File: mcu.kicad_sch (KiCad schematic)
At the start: 19 parts, among them J1 Conn_01x04, U1 STM32G473CCUx, Y1 8 MHz

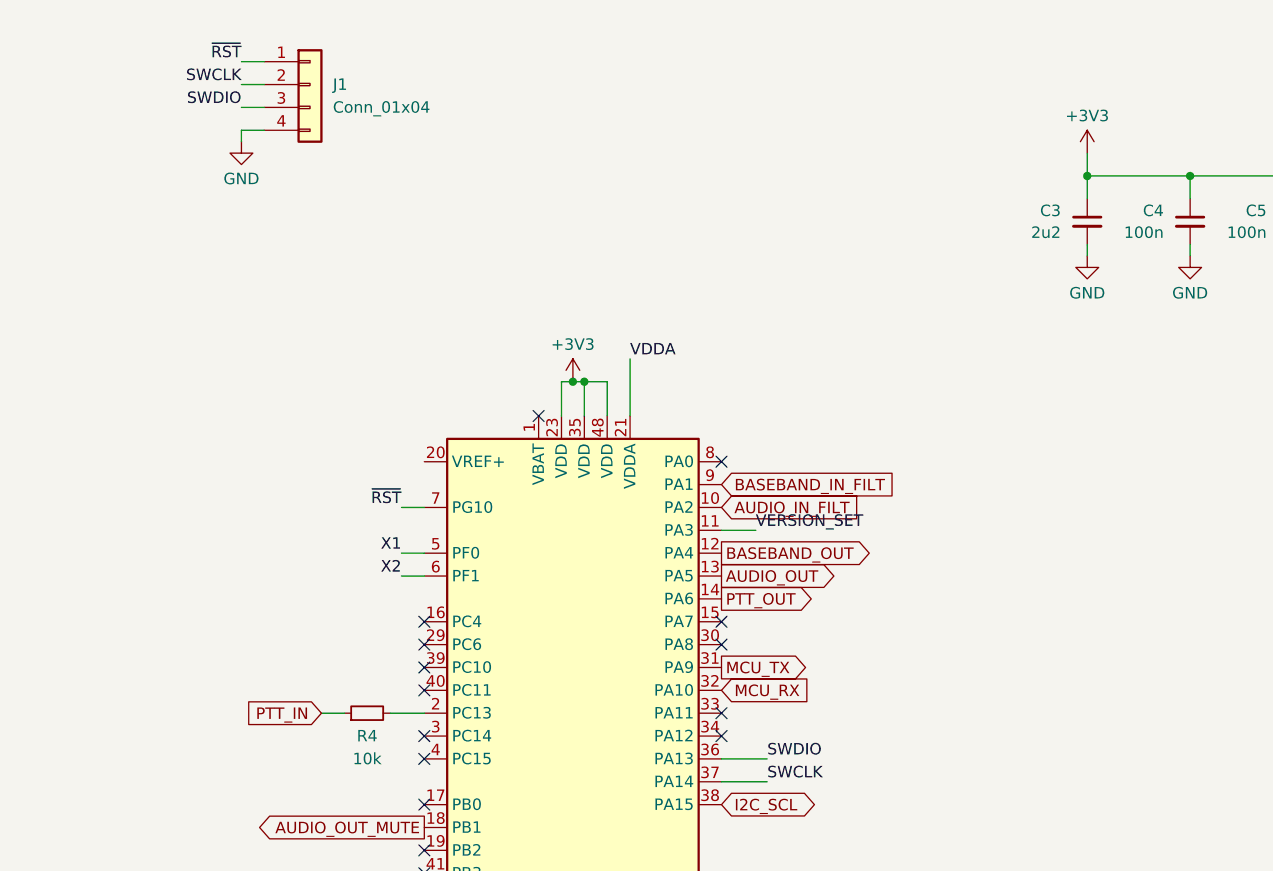
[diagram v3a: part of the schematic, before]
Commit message: Updates
GP relay added,
3v3 added to programming conn.
diode(dnp) added for motorola type internal bus.
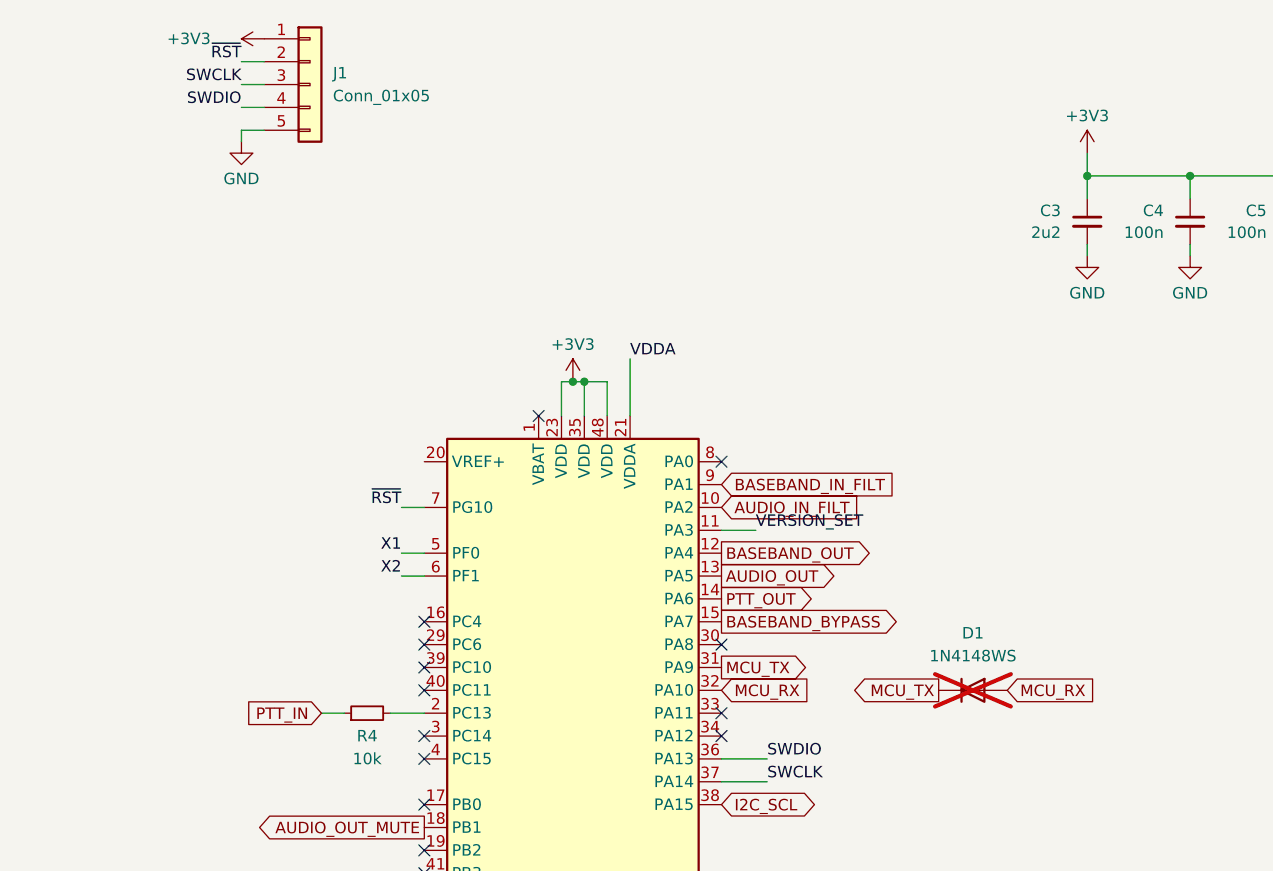
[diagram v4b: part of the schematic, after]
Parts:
- removed J1: Conn_01x04, Connector_Harwin:Harwin_M20-89004xx_1x04_P2.54mm_Horizontal, symbol Connector_Generic:Conn_01x04
- added D1: 1N4148WS, Diode_SMD:D_SOD-323, symbol Diode:1N4148WS
- added J1: Conn_01x05, Connector_Harwin:Harwin_M20-89005xx_1x05_P2.54mm_Horizontal, symbol Connector_Generic:Conn_01x05
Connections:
- net +3V3: now also J1.1 (Pin_1)
- net GND: now also J1.5 (Pin_5)
- net MCU_RX: now also D1.2 (A)
- net MCU_TX: now also D1.1 (K)
- net SWCLK: now also J1.3 (Pin_3)
- net SWDIO: now also J1.4 (Pin_4)
- net ~{RST}: now also J1.2 (Pin_2)
- net BASEBAND_BYPASS: now reaches U1.15 (PA7)
- no-connect marks 25 -> 24
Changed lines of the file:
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@@
 	)
 	(no_connect
-		(at 154.94 83.82)
-	)
-	(no_connect
 		(at 121.92 121.92)
 	)
@@
 		)
 	)
+	(global_label "MCU_TX"
+		(shape output)
+		(at 179.07 91.44 180)
+		(fields_autoplaced yes)
+		(effects
+			(font
+				(size 1.27 1.27)
+			)
+			(justify right)
+		)
+		(property "Intersheetrefs" "${INTERSHEET_REFS}"
+			(at 168.8882 91.44 0)
+			(effects
+				(font
+					(size 1.27 1.27)
+				)
+				(justify right)
+				(hide yes)
+			)
+		)
+	)
+	(global_label "BASEBAND_BYPASS"
+		(shape output)
+		(at 154.94 83.82 0)
+		(fields_autoplaced yes)
+		(effects
+			(font
+				(size 1.27 1.27)
+			)
+			(justify left)
+		)
+		(property "Intersheetrefs" "${INTERSHEET_REFS}"
+			(at 175.7052 83.82 0)
+			(effects
+				(font
+					(size 1.27 1.27)
+				)
+				(justify left)
+				(hide yes)
+			)
+		)
+	)
 	(global_label "AUDIO_OUT_MUTE"
 		(shape output)
@@
 		)
 	)
+	(global_label "MCU_RX"
+		(shape input)
+		(at 186.69 91.44 0)
+		(fields_autoplaced yes)
+		(effects
+			(font
+				(size 1.27 1.27)
+			)
+			(justify left)
+		)
+		(property "Intersheetrefs" "${INTERSHEET_REFS}"
+			(at 197.1742 91.44 0)
+			(effects
+				(font
+					(size 1.27 1.27)
+				)
+				(justify left)
+				(hide yes)
+			)
+		)
+	)
 	(global_label "PTT_IN"
 		(shape input)
@@
 		(at 170.18 190.5 0)
 		(unit 1)
-		(exclude_from_sim no)
+		(exclude_from_sim yes)
 		(in_bom no)
 		(on_board yes)
@@
 			)
 		)
-		(property "Sim.Enable" "0"
-			(at 170.18 190.5 0)
+		(instances
+			(project "micro17"
+				(path "/8b0d7f56-1962-40c9-8b95-6d4fe558acbc/9f9e0b5b-f07d-4ebd-b315-be375c62719d"
+					(reference "SYM1")
+					(unit 1)
+				)
+			)
+		)
+	)
+	(symbol
+		(lib_id "Diode:1N4148WS")
+		(at 182.88 91.44 0)
+		(unit 1)
+		(exclude_from_sim no)
+		(in_bom yes)
+		(on_board yes)
+		(dnp yes)
+		(fields_autoplaced yes)
+		(property "Reference" "D1"
+			(at 182.88 85.09 0)
+			(effects
+				(font
+					(size 1.27 1.27)
+				)
+			)
+		)
+		(property "Value" "1N4148WS"
+			(at 182.88 87.63 0)
+			(effects
+				(font
+					(size 1.27 1.27)
+				)
+			)
+		)
+		(property "Footprint" "Diode_SMD:D_SOD-323"
+			(at 182.88 95.885 0)
+			(effects
+				(font
+					(size 1.27 1.27)
+				)
+				(hide yes)
+			)
+		)
+		(property "Datasheet" "https://www.vishay.com/docs/85751/1n4148ws.pdf"
+			(at 182.88 91.44 0)
+			(effects
+				(font
+					(size 1.27 1.27)
+				)
+				(hide yes)
+			)
+		)
+		(property "Description" "75V 0.15A Fast switching Diode, SOD-323"
+			(at 182.88 91.44 0)
+			(effects
+				(font
+					(size 1.27 1.27)
+				)
+				(hide yes)
+			)
+		)
+		(property "Sim.Device" "D"
+			(at 182.88 91.44 0)
+			(effects
+				(font
+					(size 1.27 1.27)
+				)
+				(hide yes)
+			)
+		)
+		(property "Sim.Pins" "1=K 2=A"
+			(at 182.88 91.44 0)
 			(effects
 				(font
@@
 			)
 		)
+		(pin "2"
+		)
+		(pin "1"
+		)
 		(instances
 			(project "micro17"
 				(path "/8b0d7f56-1962-40c9-8b95-6d4fe558acbc/9f9e0b5b-f07d-4ebd-b315-be375c62719d"
-					(reference "SYM1")
+					(reference "D1")
 					(unit 1)
 				)
@@
 	)
 	(symbol
+		(lib_id "Connector_Generic:Conn_01x05")
+		(at 109.22 24.13 0)
+		(unit 1)
+		(exclude_from_sim no)
+		(in_bom yes)
+		(on_board yes)
+		(dnp no)
+		(fields_autoplaced yes)
+		(property "Reference" "J1"
+			(at 111.76 22.8599 0)
+			(effects
+				(font
+					(size 1.27 1.27)
+				)
+				(justify left)
+			)
+		)
+		(property "Value" "Conn_01x05"
+			(at 111.76 25.3999 0)
+			(effects
+				(font
+					(size 1.27 1.27)
+				)
+				(justify left)
+			)
+		)
+		(property "Footprint" "Connector_Harwin:Harwin_M20-89005xx_1x05_P2.54mm_Horizontal"
+			(at 109.22 24.13 0)
+			(effects
+				(font
+					(size 1.27 1.27)
+				)
+				(hide yes)
+			)
+		)
+		(property "Datasheet" "~"
+			(at 109.22 24.13 0)
+			(effects
+				(font
+					(size 1.27 1.27)
+				)
+				(hide yes)
+			)
+		)
+		(property "Description" "Generic connector, single row, 01x05, script generated (kicad-library-utils/schlib/autogen/connector/)"
+			(at 109.22 24.13 0)
+			(effects
+				(font
+					(size 1.27 1.27)
+				)
+				(hide yes)
+			)
+		)
+		(pin "3"
+		)
+		(pin "5"
+		)
+		(pin "2"
+		)
+		(pin "4"
+		)
+		(pin "1"
+		)
+		(instances
+			(project "micro17"
+				(path "/8b0d7f56-1962-40c9-8b95-6d4fe558acbc/9f9e0b5b-f07d-4ebd-b315-be375c62719d"
+					(reference "J1")
+					(unit 1)
+				)
+			)
+		)
+	)
+	(symbol
 		(lib_id "power:GND")
 		(at 252.73 43.18 0)
@@
 		(at 158.75 190.5 0)
 		(unit 1)
-		(exclude_from_sim no)
+		(exclude_from_sim yes)
 		(in_bom no)
 		(on_board yes)
@@
 			)
 		)
-		(property "Sim.Enable" "0"
-			(at 158.75 190.5 0)
-			(effects
-				(font
-					(size 1.27 1.27)
-				)
-				(hide yes)
-			)
-		)
 		(instances
 			(project "micro17"
@@
 	)
 	(symbol
-		(lib_id "Connector_Generic:Conn_01x04")
-		(at 109.22 24.13 0)
-		(unit 1)
-		(exclude_from_sim no)
-		(in_bom yes)
-		(on_board yes)
-		(dnp no)
-		(fields_autoplaced yes)
-		(property "Reference" "J1"
-			(at 111.76 24.1299 0)
-			(effects
-				(font
-					(size 1.27 1.27)
-				)
-				(justify left)
-			)
-		)
-		(property "Value" "Conn_01x04"
-			(at 111.76 26.6699 0)
-			(effects
-				(font
-					(size 1.27 1.27)
-				)
-				(justify left)
-			)
-		)
-		(property "Footprint" "Connector_Harwin:Harwin_M20-89004xx_1x04_P2.54mm_Horizontal"
-			(at 109.22 24.13 0)
-			(effects
-				(font
-					(size 1.27 1.27)
-				)
-				(hide yes)
-			)
-		)
-		(property "Datasheet" "~"
-			(at 109.22 24.13 0)
-			(effects
-				(font
-					(size 1.27 1.27)
-				)
-				(hide yes)
-			)
-		)
-		(property "Description" "Generic connector, single row, 01x04, script generated (kicad-library-utils/schlib/autogen/connector/)"
-			(at 109.22 24.13 0)
-			(effects
-				(font
-					(size 1.27 1.27)
-				)
-				(hide yes)
-			)
-		)
-		(pin "4"
-		)
-		(pin "2"
-		)
-		(pin "3"
-		)
-		(pin "1"
-		)
-		(instances
-			(project "micro17"
-				(path "/8b0d7f56-1962-40c9-8b95-6d4fe558acbc/9f9e0b5b-f07d-4ebd-b315-be375c62719d"
-					(reference "J1")
-					(unit 1)
-				)
-			)
-		)
-	)
-	(symbol
 		(lib_id "Device:C_Small")
 		(at 54.61 55.88 0)
@@
 					(unit 1)
 				)
+			)
+		)
+	)
+	(symbol
+		(lib_id "power:+3V3")
+		(at 104.14 19.05 90)
+		(unit 1)
+		(exclude_from_sim no)
+		(in_bom yes)
+		(on_board yes)
+		(dnp no)
+		(property "Reference" "#PWR025"
+			(at 107.95 19.05 0)
+			(effects
+				(font
+					(size 1.27 1.27)
+				)
+				(hide yes)
+			)
+		)
+		(property "Value" "+3V3"
+			(at 95.758 19.05 90)
+			(effects
+				(font
+					(size 1.27 1.27)
+				)
+			)
+		)
+		(property "Footprint" ""
+			(at 104.14 19.05 0)
+			(effects
+				(font
+					(size 1.27 1.27)
+				)
+				(hide yes)
+			)
+		)
+		(property "Datasheet" ""
+			(at 104.14 19.05 0)
+			(effects
+				(font
+					(size 1.27 1.27)
+				)
+				(hide yes)
+			)
+		)
+		(property "Description" ""
+			(at 104.14 19.05 0)
+			(effects
+				(font
+					(size 1.27 1.27)
+				)
+				(hide yes)
+			)
+		)
+		(pin "1"
+		)
+		(instances
+			(project "micro17"
+				(path "/8b0d7f56-1962-40c9-8b95-6d4fe558acbc/9f9e0b5b-f07d-4ebd-b315-be375c62719d"
+					(reference "#PWR025")
+					(unit 1)
+				)

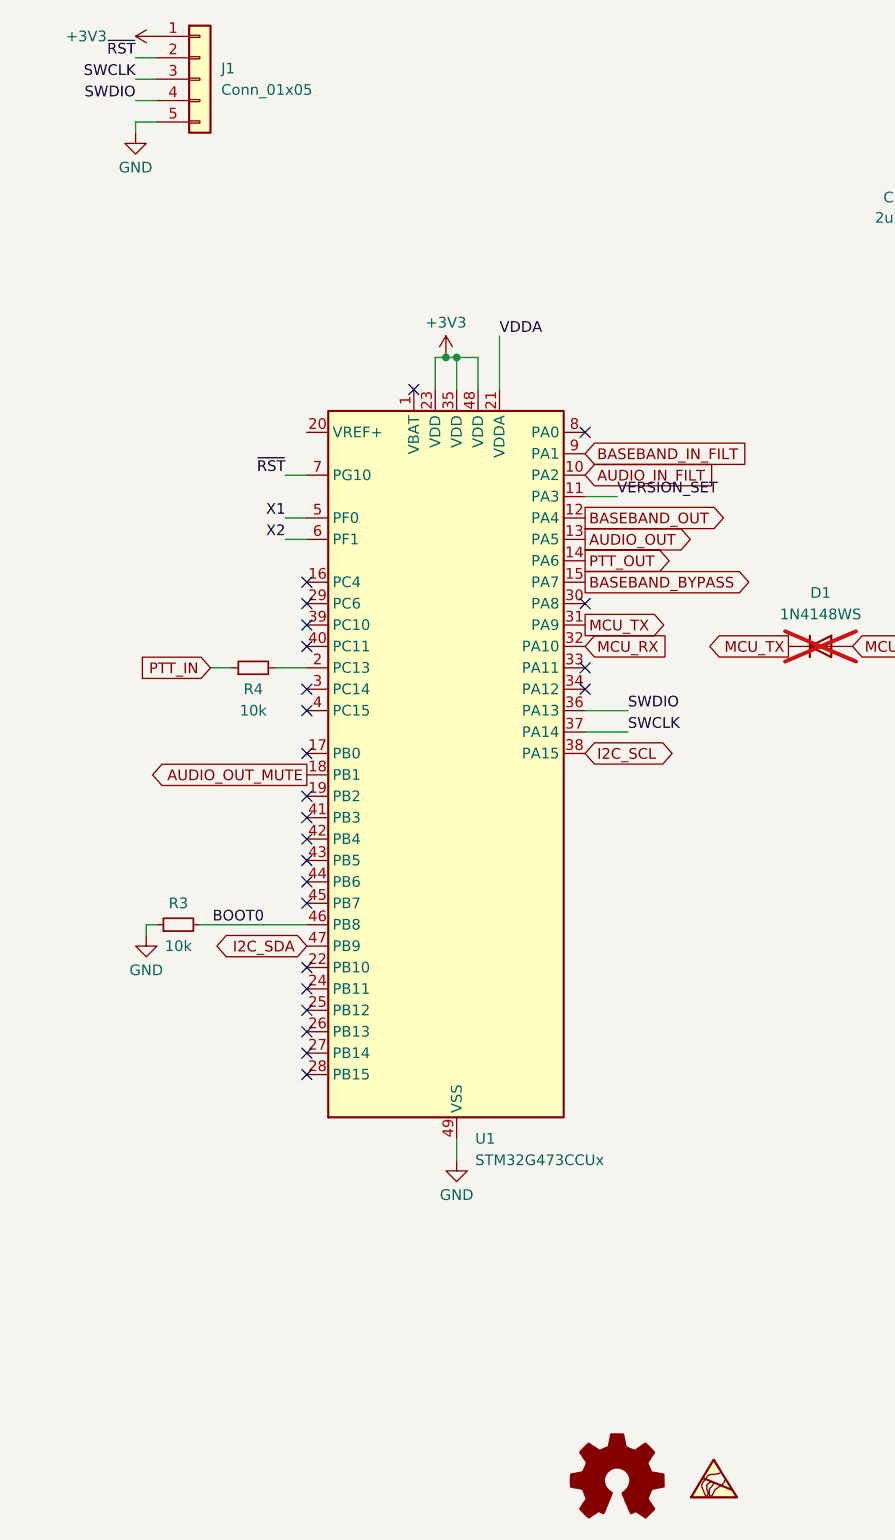
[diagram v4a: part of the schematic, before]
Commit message: LCSC part numbers included into schematics
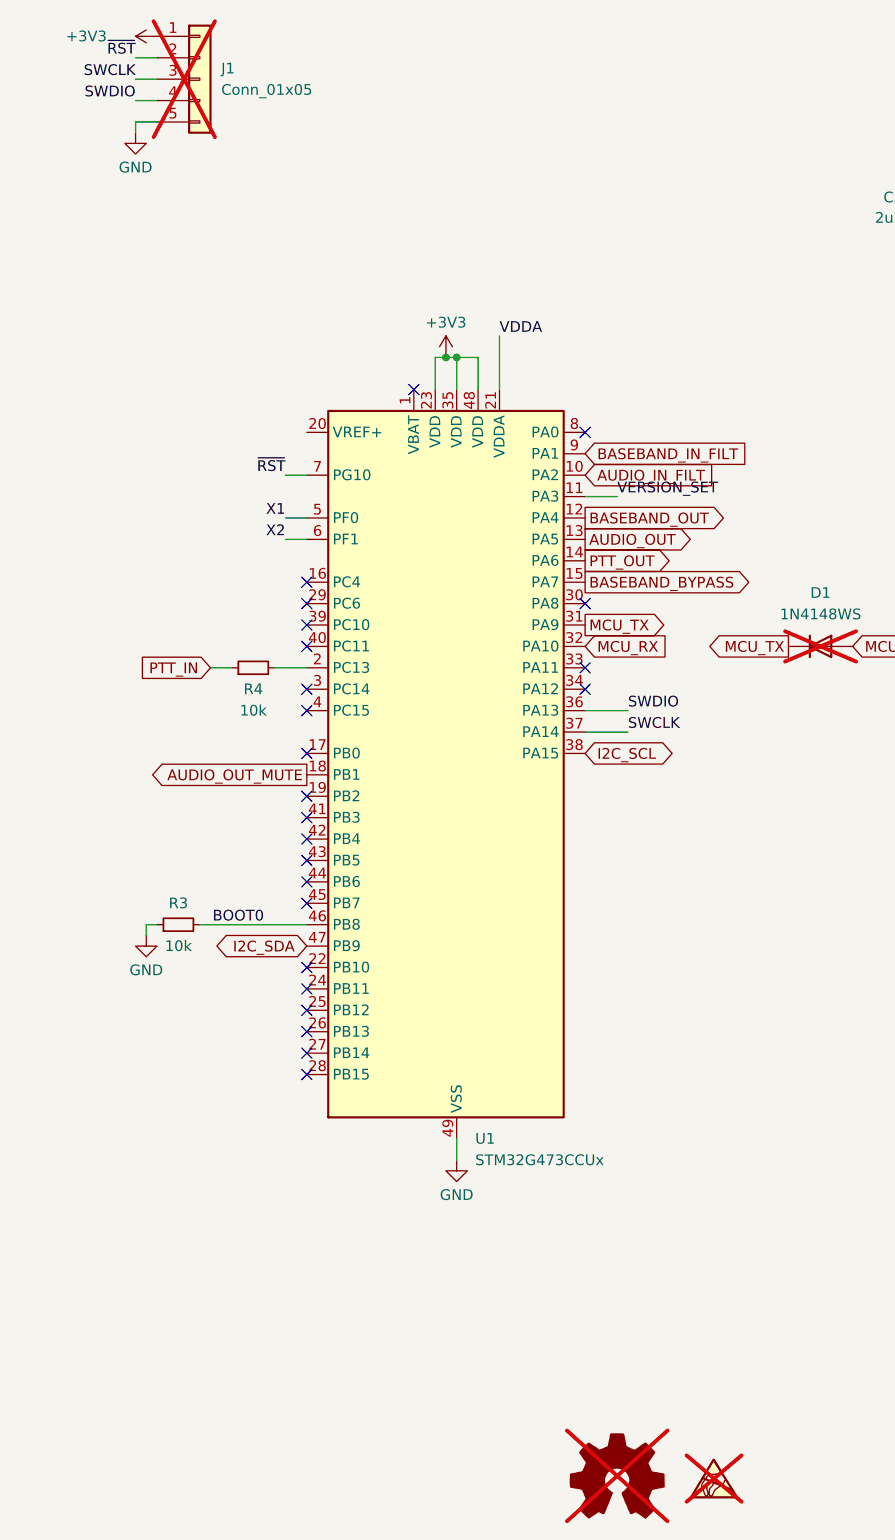
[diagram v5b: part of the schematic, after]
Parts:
- C1, C2: LCSC (none) -> C1559
- C3: LCSC (none) -> C170151
- C4, C5, C6, C7, C8: LCSC (none) -> C56392
- C9: LCSC (none) -> C29266
- J1, SYM1, SYM2: now not fitted
- R1: LCSC (none) -> C4354982
- R2: LCSC (none) -> C25752
- R3, R4: LCSC (none) -> C102749
- R5: LCSC (none) -> C854481
- U1: LCSC (none) -> C1342773
- Y1: LCSC (none) -> C5308002; LCSC Part# C5308002 -> (none)
